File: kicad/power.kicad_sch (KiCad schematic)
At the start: 25 parts, among them U1 MAX77540AAWV+T, U3 TCKE812NA,RF, U8 FPF3042UCX

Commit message: Connected all remaining unconnected pins
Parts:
- L?: value .47µH -> 0.47µH
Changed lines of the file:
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@@
     (in_bom yes) (on_board yes)
     (property "Reference" "L?" (id 0) (at 176.53 106.68 0))
-    (property "Value" ".47µH" (id 1) (at 176.53 109.22 0))
+    (property "Value" "0.47µH" (id 1) (at 176.53 109.22 0))
     (property "Footprint" "" (id 2) (at 171.45 109.22 0)
       (effects (font (size 1.27 1.27)) hide)

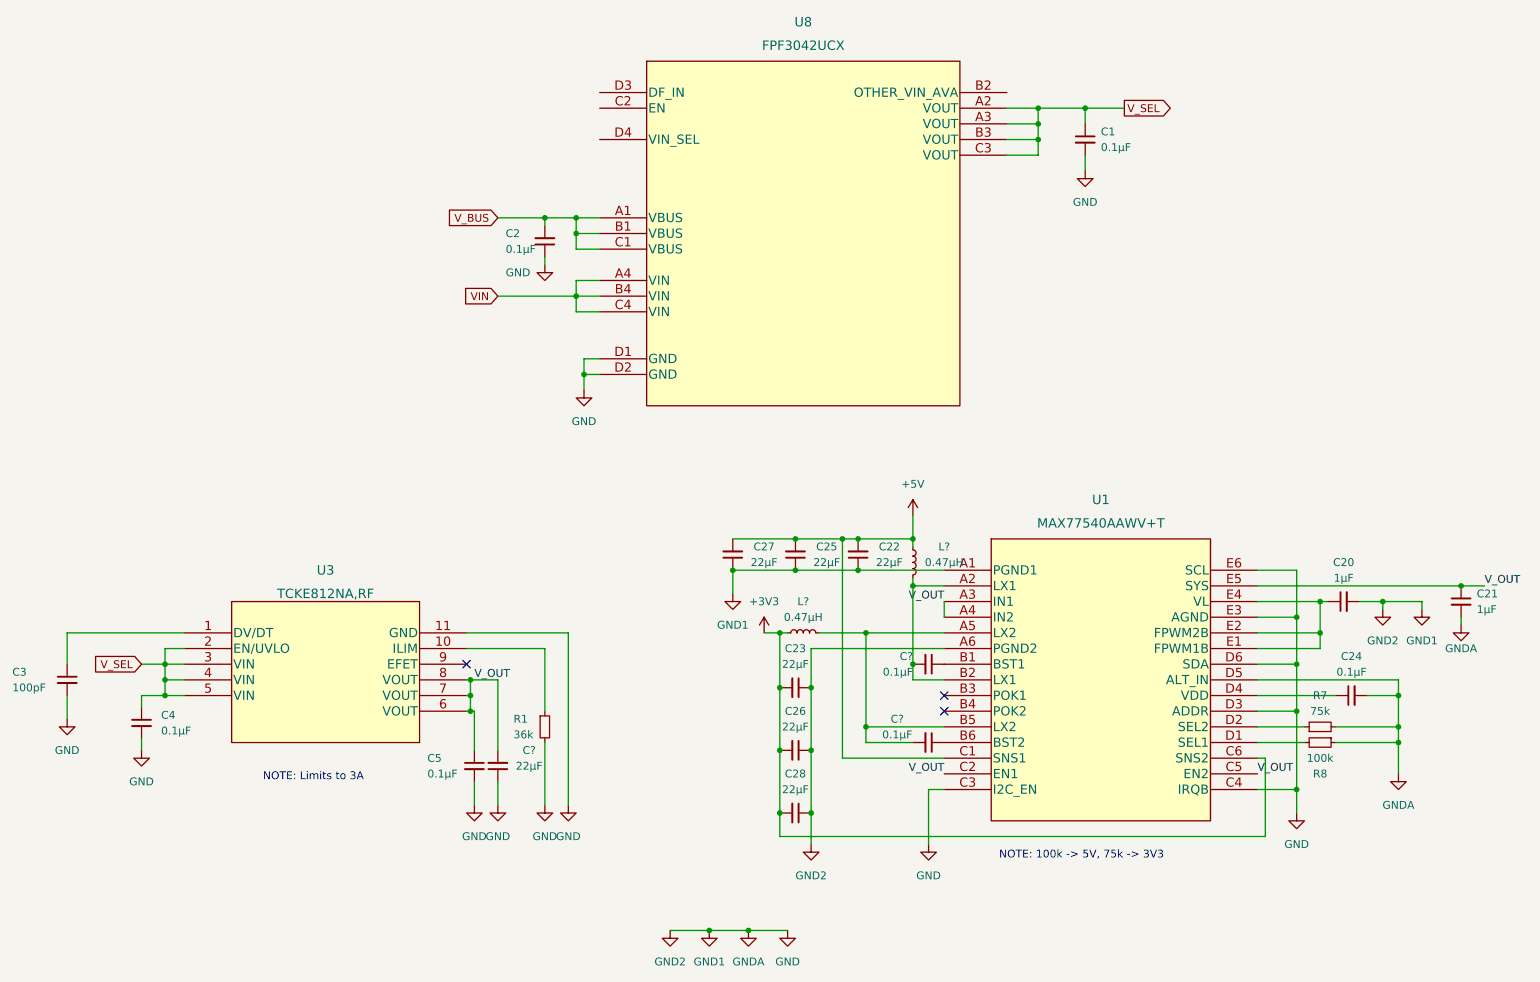
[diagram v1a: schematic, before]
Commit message: Updated schematic with various changes
Increased size of small components
Updated title/spec sheet
Cleaned footprints
Other small changes as well
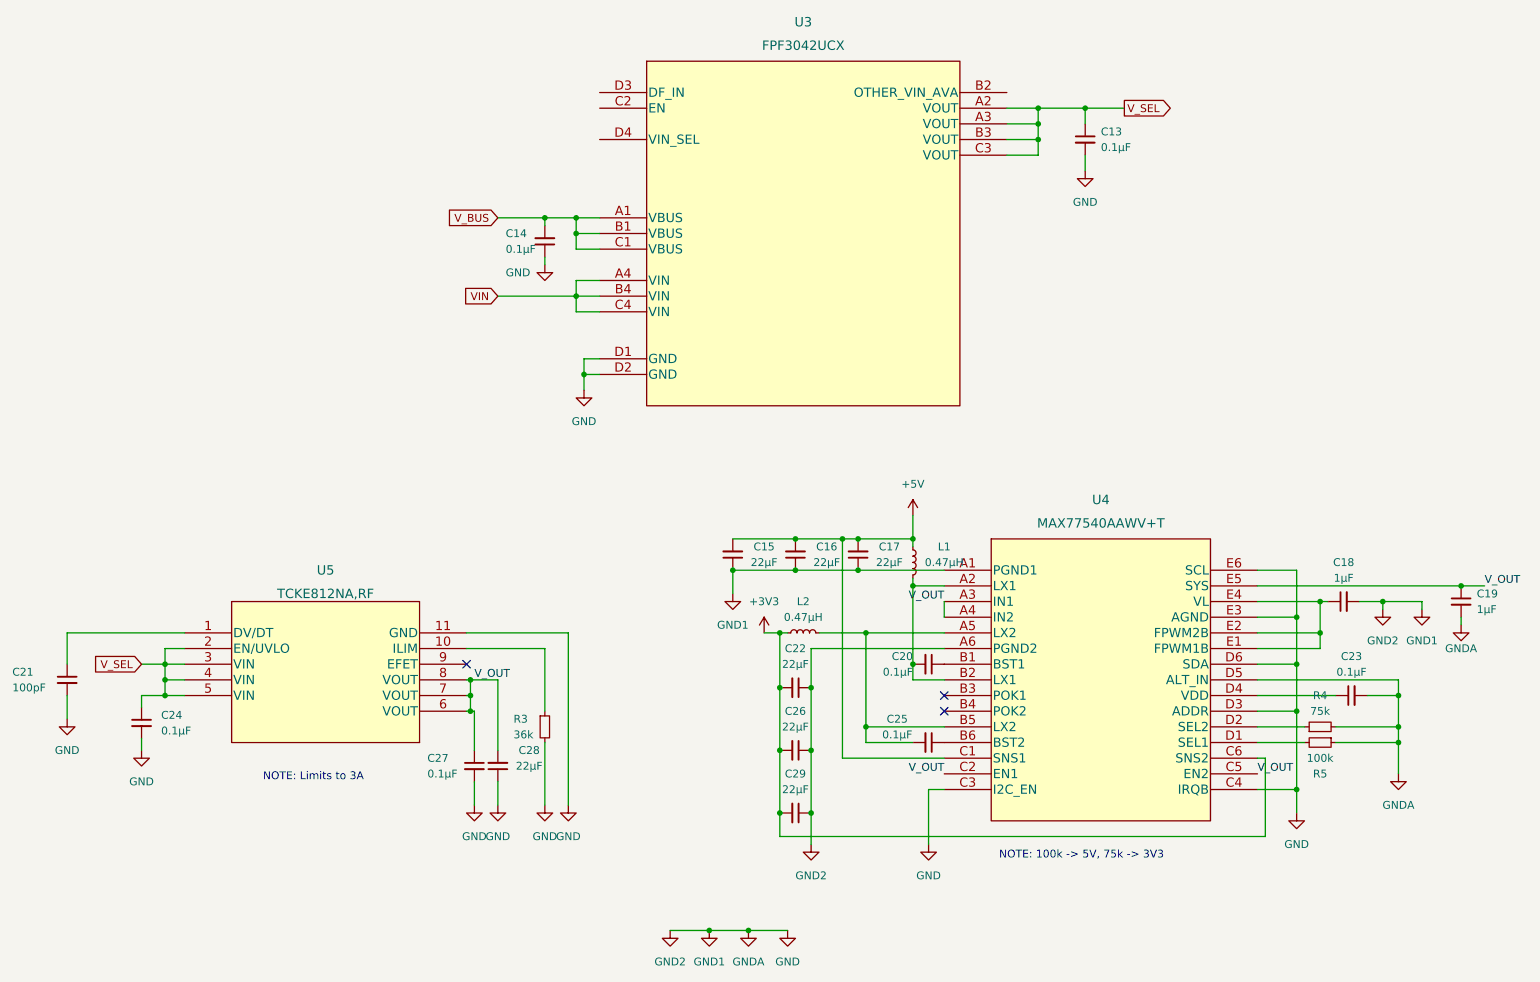
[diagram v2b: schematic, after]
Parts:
- C13: renamed from C1; footprint personal:C_0201_0603Metric -> personal:C_0402_1005Metric
- C14: renamed from C2; footprint personal:C_0201_0603Metric -> personal:C_0402_1005Metric
- C18: renamed from C20; footprint personal:C_0201_0603Metric -> personal:C_0402_1005Metric
- C19: renamed from C21; footprint personal:C_0201_0603Metric -> personal:C_0402_1005Metric
- C20, C25, C28: renamed from C?; footprint (none) -> personal:C_0402_1005Metric
- C21: renamed from C3; footprint personal:C_0201_0603Metric -> personal:C_0402_1005Metric
- C23: renamed from C24; footprint personal:C_0201_0603Metric -> personal:C_0402_1005Metric
- C24: renamed from C4; footprint personal:C_0201_0603Metric -> personal:C_0402_1005Metric
- C27: renamed from C5; footprint personal:C_0201_0603Metric -> personal:C_0402_1005Metric
- L1, L2: renamed from L?; footprint (none) -> Inductor_SMD:L_0402_1005Metric
- R3: renamed from R1; footprint personal:R_0201_0603Metric -> personal:R_0402_1005Metric
- R4: renamed from R7; footprint personal:R_0201_0603Metric -> personal:R_0402_1005Metric
- R5: renamed from R8; footprint personal:R_0201_0603Metric -> personal:R_0402_1005Metric
- renumbered C27 to C15, C25 to C16, C22 to C17, C23 to C22, C28 to C29, U8 to U3, U1 to U4, U3 to U5
